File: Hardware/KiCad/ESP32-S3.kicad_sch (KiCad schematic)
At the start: 33 parts, among them J1 UJ20-C-H-G-SMT-1-P16-TR, J4 RJ45, J5 Conn_TagConnect_TC2030-NL_ESP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, U1 ESP32-S3-WROOM-1, U5 WE-TVS-82400102, U7 AP7333-33SRG-7

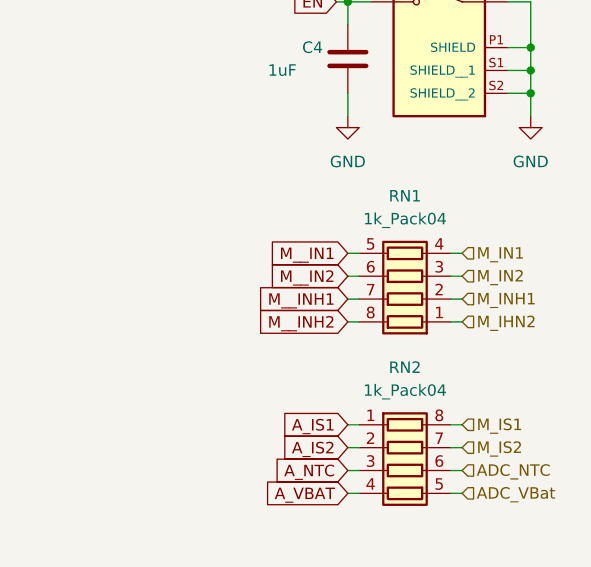
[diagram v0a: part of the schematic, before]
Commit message: update PCB, routing and Connector
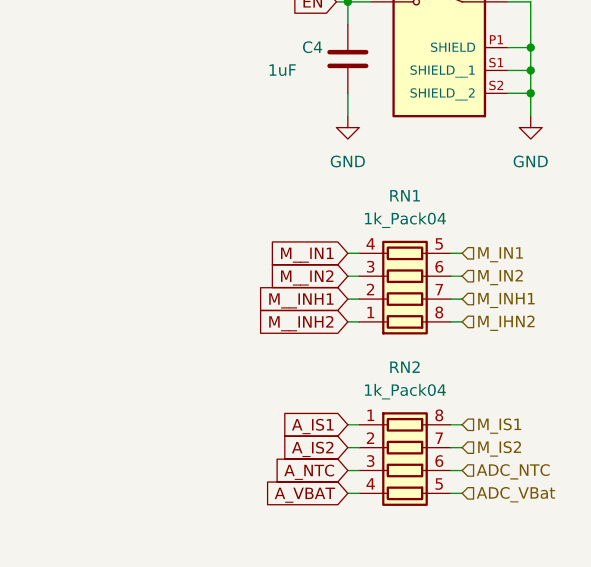
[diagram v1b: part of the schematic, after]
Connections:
- net M_IHN2: now also RN1.8 (R1.2); no longer RN1.1 (R1.1)
- net M_IN1: now also RN1.5 (R4.2); no longer RN1.4 (R4.1)
- net M_IN2: now also RN1.6 (R3.2); no longer RN1.3 (R3.1)
- net M_INH1: now also RN1.7 (R2.2); no longer RN1.2 (R2.1)
- net M__IN1: now also RN1.4 (R4.1); no longer RN1.5 (R4.2)
- net M__IN2: now also RN1.3 (R3.1); no longer RN1.6 (R3.2)
- net M__INH1: now also RN1.2 (R2.1); no longer RN1.7 (R2.2)
- net M__INH2: now also RN1.1 (R1.1); no longer RN1.8 (R1.2)
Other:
- moved on the sheet: RN1
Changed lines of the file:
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@@
     )
   )
-  (symbol (lib_id "Device:R_Pack04") (at 267.97 92.71 90) (unit 1)
-    (in_bom yes) (on_board yes) (dnp no) (fields_autoplaced)
+  (symbol (lib_id "Device:R_Pack04") (at 267.97 92.71 270) (mirror x) (unit 1)
+    (in_bom yes) (on_board yes) (dnp no)
     (property "Reference" "RN1" (at 267.97 83.82 90)
       (effects (font (size 1.27 1.27)))

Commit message: update PCB
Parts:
- U1: footprint PCM_Espressif:ESP32-S3-WROOM-1 -> BugWiper_lib:ESP32-S3-WROOM-1; symbol PCM_Espressif:ESP32-S3-WROOM-1 -> BugWiper_Lib:ESP32-S3-WROOM-1
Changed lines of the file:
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@@
     )
   )
-  (symbol (lib_id "PCM_Espressif:ESP32-S3-WROOM-1") (at 147.32 97.79 0) (unit 1)
+  (symbol (lib_id "BugWiper_Lib:ESP32-S3-WROOM-1") (at 147.32 97.79 0) (unit 1)
     (in_bom yes) (on_board yes) (dnp no)
     (property "Reference" "U1" (at 154.94 57.15 0)
@@
       (effects (font (size 1.27 1.27)) (justify left))
     )
-    (property "Footprint" "PCM_Espressif:ESP32-S3-WROOM-1" (at 149.86 146.05 0)
+    (property "Footprint" "BugWiper_lib:ESP32-S3-WROOM-1" (at 149.86 146.05 0)
       (effects (font (size 1.27 1.27)) hide)
     )

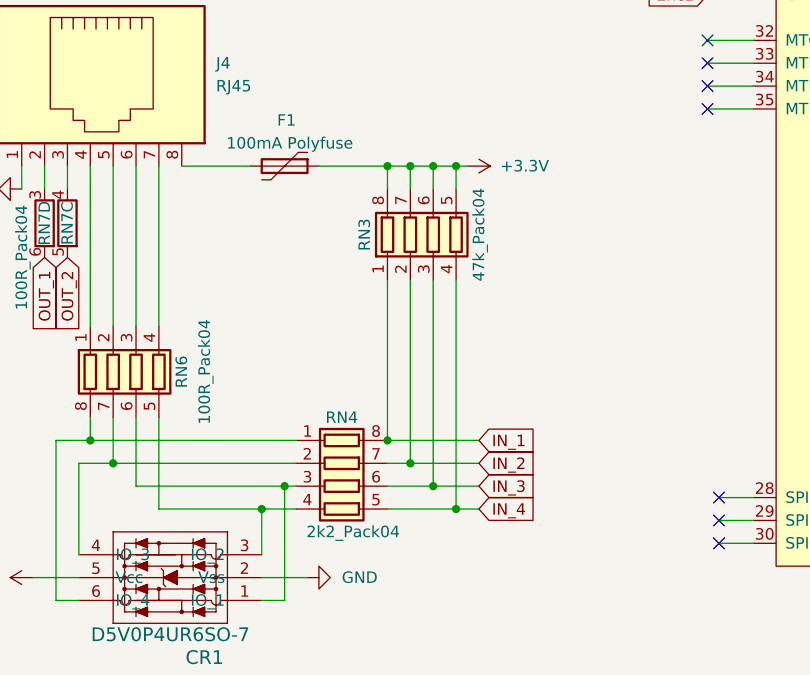
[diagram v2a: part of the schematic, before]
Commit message: delete pull-ups
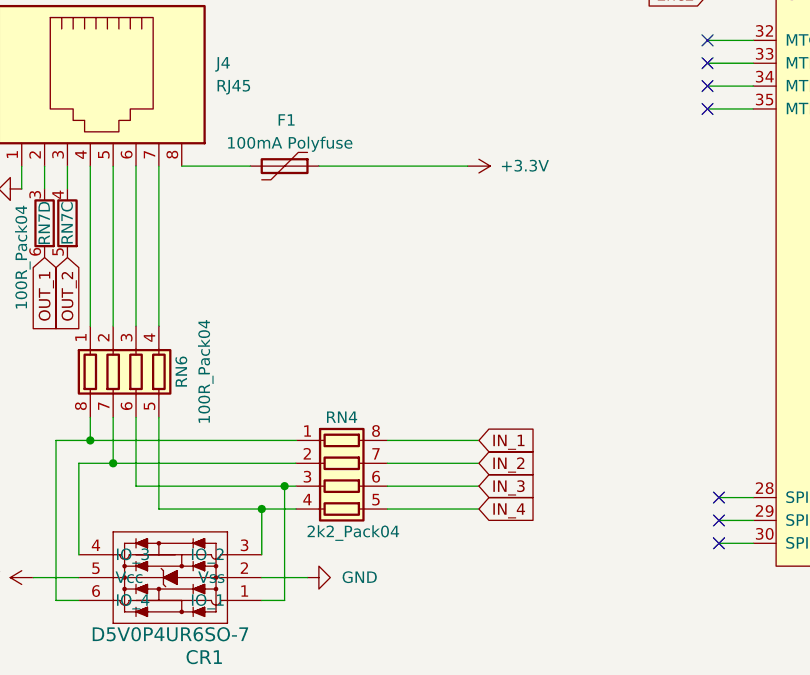
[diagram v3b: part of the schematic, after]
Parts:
- removed RN3: 47k_Pack04, BugWiper_lib:BO_CAY16, symbol Device:R_Pack04
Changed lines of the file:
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@@
   (junction (at 281.94 72.39) (diameter 0) (color 0 0 0 0)
   )
-  (junction (at 68.58 91.44) (diameter 0) (color 0 0 0 0)
-  )
   (junction (at 281.94 69.85) (diameter 0) (color 0 0 0 0)
   )
-  (junction (at 63.5 124.46) (diameter 0) (color 0 0 0 0)
-  )
-  (junction (at 66.04 127) (diameter 0) (color 0 0 0 0)
-  )
   (junction (at 147.32 54.61) (diameter 0) (color 0 0 0 0)
   )
   (junction (at 214.63 20.32) (diameter 0) (color 0 0 0 0)
   )
-  (junction (at 63.5 91.44) (diameter 0) (color 0 0 0 0)
-  )
   (junction (at 281.94 33.02) (diameter 0) (color 0 0 0 0)
   )
-  (junction (at 68.58 129.54) (diameter 0) (color 0 0 0 0)
-  )
   (junction (at 281.94 30.48) (diameter 0) (color 0 0 0 0)
   )
@@
   (junction (at 36.83 29.21) (diameter 0) (color 0 0 0 0)
   )
-  (junction (at 60.96 121.92) (diameter 0) (color 0 0 0 0)
-  )
   (junction (at 261.62 62.23) (diameter 0) (color 0 0 0 0)
   )
-  (junction (at 66.04 91.44) (diameter 0) (color 0 0 0 0)
-  )
   (junction (at 147.32 139.7) (diameter 0) (color 0 0 0 0)
   )
   (junction (at 30.48 124.46) (diameter 0) (color 0 0 0 0)
-  )
-  (junction (at 60.96 91.44) (diameter 0) (color 0 0 0 0)
   )
   (junction (at 77.47 27.94) (diameter 0) (color 0 0 0 0)
@@
     (stroke (width 0) (type default))
   )
-  (wire (pts (xy 66.04 104.14) (xy 66.04 127))
-    (stroke (width 0) (type default))
-  )
   (wire (pts (xy 281.94 72.39) (xy 281.94 74.93))
     (stroke (width 0) (type default))
@@
     (stroke (width 0) (type default))
   )
-  (wire (pts (xy 63.5 91.44) (xy 66.04 91.44))
-    (stroke (width 0) (type default))
-  )
-  (wire (pts (xy 60.96 127) (xy 66.04 127))
-    (stroke (width 0) (type default))
-  )
-  (wire (pts (xy 66.04 91.44) (xy 66.04 93.98))
+  (wire (pts (xy 60.96 127) (xy 71.12 127))
     (stroke (width 0) (type default))
   )
@@
     (stroke (width 0) (type default))
   )
-  (wire (pts (xy 60.96 124.46) (xy 63.5 124.46))
+  (wire (pts (xy 60.96 124.46) (xy 71.12 124.46))
     (stroke (width 0) (type default))
   )
@@
     (stroke (width 0) (type default))
   )
-  (wire (pts (xy 60.96 129.54) (xy 68.58 129.54))
-    (stroke (width 0) (type default))
-  )
   (wire (pts (xy 250.19 139.7) (xy 252.73 139.7))
     (stroke (width 0) (type default))
@@
     (stroke (width 0) (type default))
   )
-  (wire (pts (xy 60.96 91.44) (xy 60.96 93.98))
-    (stroke (width 0) (type default))
-  )
   (wire (pts (xy 274.32 95.25) (xy 273.05 95.25))
     (stroke (width 0) (type default))
@@
     (stroke (width 0) (type default))
   )
-  (wire (pts (xy 63.5 104.14) (xy 63.5 124.46))
-    (stroke (width 0) (type default))
-  )
   (wire (pts (xy 22.86 91.44) (xy 22.86 93.98))
     (stroke (width 0) (type default))
@@
     (stroke (width 0) (type default))
   )
-  (wire (pts (xy 68.58 91.44) (xy 68.58 93.98))
-    (stroke (width 0) (type default))
-  )
   (wire (pts (xy 261.62 59.69) (xy 261.62 62.23))
     (stroke (width 0) (type default))
@@
     (stroke (width 0) (type default))
   )
-  (wire (pts (xy 66.04 91.44) (xy 68.58 91.44))
-    (stroke (width 0) (type default))
-  )
   (wire (pts (xy 91.44 35.56) (xy 92.71 35.56))
     (stroke (width 0) (type default))
@@
     (stroke (width 0) (type default))
   )
-  (wire (pts (xy 69.85 91.44) (xy 68.58 91.44))
-    (stroke (width 0) (type default))
-  )
   (wire (pts (xy 281.94 69.85) (xy 281.94 72.39))
     (stroke (width 0) (type default))
@@
     (stroke (width 0) (type default))
   )
-  (wire (pts (xy 68.58 104.14) (xy 68.58 129.54))
-    (stroke (width 0) (type default))
-  )
   (wire (pts (xy 193.04 90.17) (xy 201.93 90.17))
     (stroke (width 0) (type default))
@@
     (stroke (width 0) (type default))
   )
-  (wire (pts (xy 68.58 129.54) (xy 71.12 129.54))
+  (wire (pts (xy 60.96 129.54) (xy 71.12 129.54))
     (stroke (width 0) (type default))
   )
@@
     (stroke (width 0) (type default))
   )
-  (wire (pts (xy 63.5 91.44) (xy 63.5 93.98))
-    (stroke (width 0) (type default))
-  )
   (wire (pts (xy 193.04 80.01) (xy 201.93 80.01))
     (stroke (width 0) (type default))
@@
     (stroke (width 0) (type default))
   )
-  (wire (pts (xy 66.04 127) (xy 71.12 127))
-    (stroke (width 0) (type default))
-  )
   (wire (pts (xy 30.48 91.44) (xy 30.48 109.22))
     (stroke (width 0) (type default))
@@
     (stroke (width 0) (type default))
   )
-  (wire (pts (xy 63.5 124.46) (xy 71.12 124.46))
-    (stroke (width 0) (type default))
-  )
   (wire (pts (xy 24.13 121.92) (xy 24.13 139.7))
     (stroke (width 0) (type default))
@@
     (stroke (width 0) (type default))
   )
-  (wire (pts (xy 53.34 91.44) (xy 60.96 91.44))
-    (stroke (width 0) (type default))
-  )
   (wire (pts (xy 152.4 54.61) (xy 147.32 54.61))
     (stroke (width 0) (type default))
@@
     (stroke (width 0) (type default))
   )
-  (wire (pts (xy 60.96 104.14) (xy 60.96 121.92))
-    (stroke (width 0) (type default))
-  )
   (wire (pts (xy 49.53 127) (xy 50.8 127))
     (stroke (width 0) (type default))
@@
     (stroke (width 0) (type default))
   )
-  (wire (pts (xy 60.96 91.44) (xy 63.5 91.44))
+  (wire (pts (xy 53.34 91.44) (xy 69.85 91.44))
     (stroke (width 0) (type default))
   )
@@
         )
       )
-    )
-  )
-  (symbol (lib_id "Device:R_Pack04") (at 66.04 99.06 0) (unit 1)
-    (in_bom yes) (on_board yes) (dnp no)
-    (property "Reference" "RN3" (at 58.42 99.06 90)
-      (effects (font (size 1.27 1.27)))
-    )
-    (property "Value" "47k_Pack04" (at 71.12 99.06 90)
-      (effects (font (size 1.27 1.27)))
-    )
-    (property "Footprint" "BugWiper_lib:BO_CAY16" (at 73.025 99.06 90)
-      (effects (font (size 1.27 1.27)) hide)
-    )
-    (property "Datasheet" "~" (at 66.04 99.06 0)
-      (effects (font (size 1.27 1.27)) hide)
-    )
-    (pin "3")
-    (pin "8")
-    (pin "2")
-    (pin "6")
-    (pin "1")
-    (pin "5")
-    (pin "4")
-    (pin "7")
-    (instances
-      (project "BugWiperPCB"
-        (path "/d31a15bd-db02-4d4c-9593-17c596d3182c/caaad550-b4dc-4462-8f3c-cac307d6a6e2"
-          (reference "RN3") (unit 1)
-        )
-      )

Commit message: routing
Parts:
- added C32, C33, C34, C35, C36, C37, C38: 10nF, Capacitor_SMD:C_0603_1608Metric, symbol Device:C
- added R14: 1k, Resistor_SMD:R_0603_1608Metric, symbol Device:R
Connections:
- net Enc1: now also C36.1
- net Enc2: now also C37.1
- net GND: now also C32.2, C33.2, C34.2, C35.2, C36.2, C37.2, C38.2
- net IN_1: now also C32.1
- net IN_2: now also C33.1
- net IN_3: now also C34.1
- net IN_4: now also C35.1
- net OUT1: now also U1.11 (GPIO18/U1RXD/ADC2_CH7/CLK_OUT3); no longer U1.12 (GPIO8/TOUCH8/ADC1_CH7/SUBSPICS1)
- net OUT2: now also U1.12 (GPIO8/TOUCH8/ADC1_CH7/SUBSPICS1); no longer U1.17 (GPIO9/TOUCH9/ADC1_CH8/FSPIHD/SUBSPIHD)
- net SW1: now reaches U1.10 (GPIO17/U1TXD/ADC2_CH6)
- net SW1: now also RN5.6 (R3.2), C38.1
- net at RN5.3 (R3.1): now also R14.1
- new net sw_1: R14.2
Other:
- moved on the sheet: CR1, CR2, F1, J4, RN4, RN5, RN6, RN7A, RN7B, RN7C, RN7D

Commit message: PCB mostly finished
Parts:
- added C39: 100nF, Capacitor_SMD:C_0603_1608Metric, symbol Device:C
- added CR3: D5V0P4UR6SO-7, BugWiper_lib:SOT26_DIO, symbol BugWiper_Lib:D5V0P4UR6SO-7
- added R15: 1k, Resistor_SMD:R_0603_1608Metric, symbol Device:R
- added RN3: 100R_Pack04, BugWiper_lib:BO_CAY16, symbol Device:R_Pack04_Split
- C38: value 10nF -> 100nF
- RN7: footprint Resistor_THT:R_Array_SIP8 -> BugWiper_lib:BO_CAY16
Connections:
- net +3.3V: now also CR3.5 (Vcc)
- net Encoder_C1: now also RN7.2 (R2.1); no longer RN7.1 (R1.1)
- net Encoder_C2: now also RN7.3 (R3.1); no longer RN7.2 (R2.1)
- net GND: now also C39.2, CR3.2 (Vss)
- net OUT1: now also R14.2, U1.17 (GPIO9/TOUCH9/ADC1_CH8/FSPIHD/SUBSPIHD); no longer U1.11 (GPIO18/U1RXD/ADC2_CH7/CLK_OUT3)
- net OUT2: now also R15.1
- net OUT_1: now also R14.1, CR3.1 (IO_1), RN3.6 (R3.2); no longer CR2.1 (IO_1), RN7.6 (R3.2)
- net OUT_2: now also CR3.3 (IO_2), R15.2, RN3.5 (R4.2); no longer CR2.3 (IO_2), RN7.5 (R4.2)
- net sw_1: now also RN7.4 (R4.1); no longer R14.2
- net at RN5.3 (R3.1): now also CR2.1 (IO_1), RN7.6 (R3.2); no longer R14.1
- net at J4.2: now also RN3.3 (R3.1); no longer RN7.3 (R3.1)
- net at J4.3: now also RN3.4 (R4.1); no longer RN7.4 (R4.1)
- net at RN5.4 (R4.1): now also CR2.3 (IO_2), RN7.5 (R4.2)
- net SW2: now reaches RN5.5 (R4.2)
- net SW2: now also U1.11 (GPIO18/U1RXD/ADC2_CH7/CLK_OUT3), C39.1
- new net sw_2: RN7.1 (R1.1)
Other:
- moved on the sheet: C36, C37, C38, CR2, RN7A, RN7B

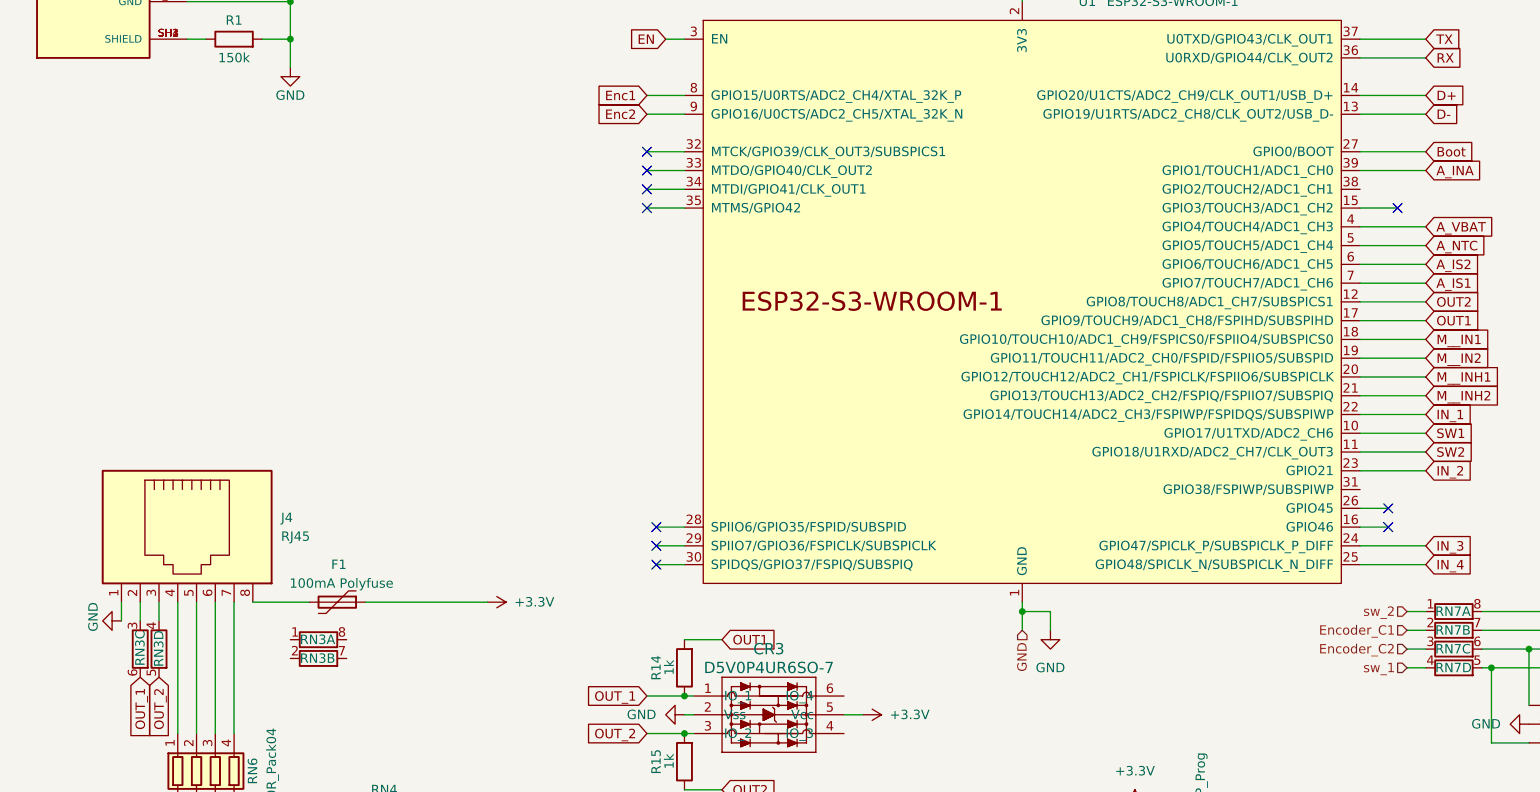
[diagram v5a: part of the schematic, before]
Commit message: Update PCB
add Connector for Sw_2, add voltage devider for the encoder
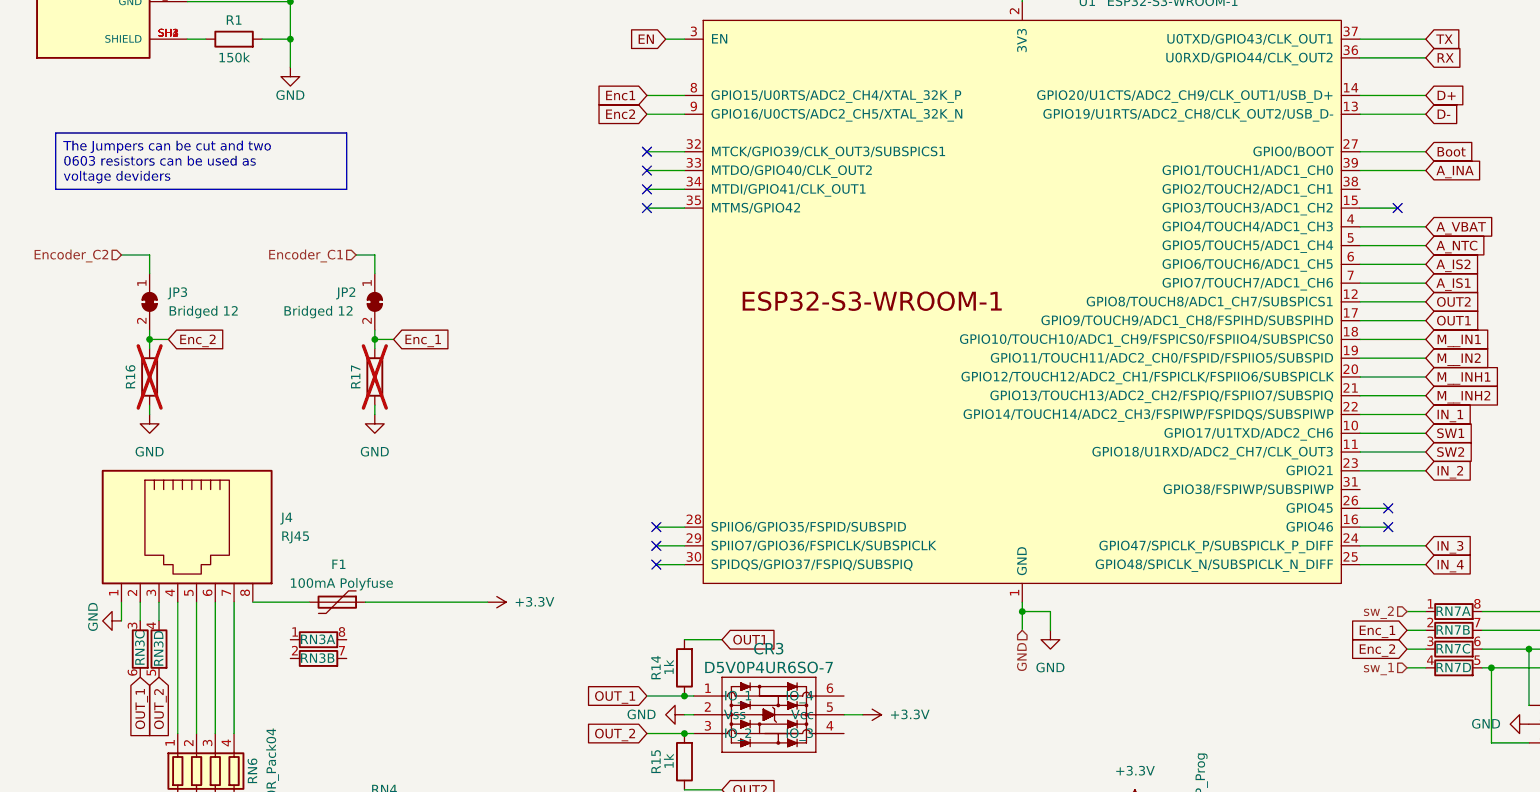
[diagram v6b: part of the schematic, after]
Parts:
- added JP2, JP3: Bridged 12, BugWiper_lib:SolderJumper_2P_R_SMD_0603_Bridged, symbol BugWiper_Lib:SolderJumper_2_Bridged
- added R16, R17: ~, Resistor_SMD:R_0603_1608Metric, symbol Device:R
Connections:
- net Encoder_C1: now also JP2.1 (A); no longer RN7.2 (R2.1)
- net Encoder_C2: now also JP3.1 (A); no longer RN7.3 (R3.1)
- net GND: now also R16.1, R17.1
- new net Enc_1: JP2.2 (A), R17.2, RN7.2 (R2.1)
- new net Enc_2: JP3.2 (A), R16.2, RN7.3 (R3.1)
